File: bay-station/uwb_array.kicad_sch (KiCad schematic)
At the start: 16 parts, among them U4 DW3210, U5 DW3210, U6 DW3210, U7 DW3210

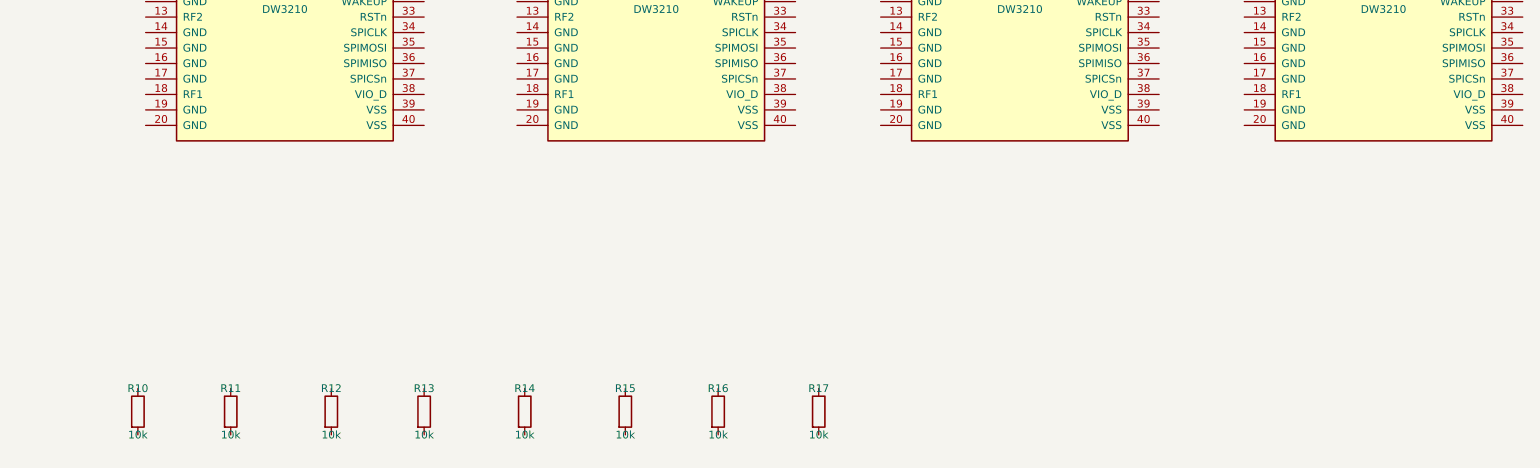
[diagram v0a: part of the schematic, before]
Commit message: Import the DW3210 filtering set from Qorvo's reference design
43 components onto uwb_array.kicad_sch: full per-anchor decoupling, RF1 DC
blocks, RF2 terminations and VDD2a ferrite beads. Placement only, matching
the rest of this board. The sheet previously had 16 components and not one
capacitor.

All values come from the real Qorvo DW3000 Datasheet v1.1, Figure 32
"DW3000 WLCSP Application Circuit" -- Qorvo's own reference design. Figure 32
is an image, so none of it extracts as text; it was read by rendering the
page. Per anchor:

  100nF  VDD1 (29) + VDD2b (23)        [Fig32 C5]
  FB     BLM03PG330SN1D -> VDD2a (28)  [Fig32 FB1]
  4.7nF  VDD2a (28), at the pad        [Fig32 C1]
  4.7nF + 100nF + 10uF  VDD3 (26)      [Fig32 C10/C11/C12]
  220nF  VTX_D (27), cap to GND only   [Fig32 C9]
  100nF  VIO_D (38), cap to GND only   [Fig32 C21]
  2.0pF  RF1 (18) series DC block      [Fig32 C2]
  49R9   RF2 (13) termination          [Fig32 R1, DW3110 inset]

plus a shared +3V3 rail bank of 10uF/100nF/4.7nF [Fig32 C6/C7/C8].

Refdes run in consecutive blocks per anchor: U4 = C40-C47, U5 = C48-C55,
U6 = C56-C63, U7 = C64-C71, rail = C72-C74, beads FB1-FB4, terminations
R33-R36. The table in docs/passives-reference.md was generated from the
file and cross-checked against it, not written by hand.

Two judgment calls worth flagging:

- **The ferrite bead is per anchor, not one on the rail.** Figure 32 shows
  one because it shows one chip. Four transceivers sharing a supply is a
  different problem: a bead each keeps one anchor's TX transient out of the
  others' references, on a board whose product is timestamp accuracy.
- **The 2.0pF on RF1 is not an ordinary DC block** and must not be
  "improved". Qorvo: "these capacitors are a part of the RF transmission
  line, this line was simulated in design and this capacitance value was
  chosen as the result of the simulation." Section 7.3 requires its pads be
  embedded in the track at track width.

Deliberately NOT placed: Figure 3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
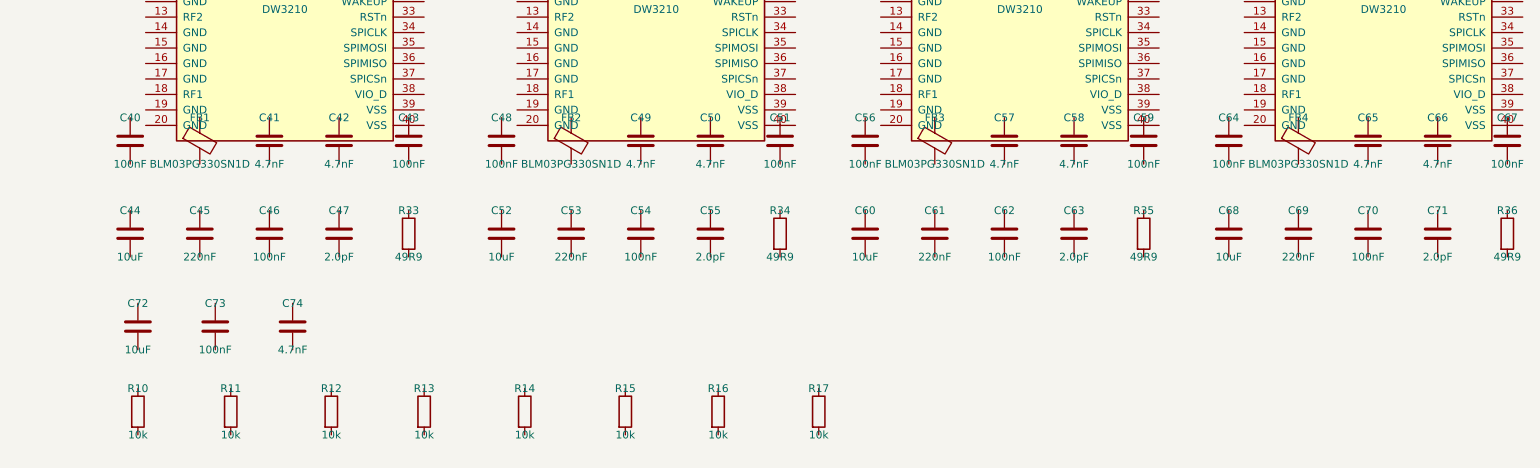
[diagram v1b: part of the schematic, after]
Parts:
- added C40, C43, C46, C48, C51, C54, C56, C59, C62, C64, C67, C70, C73: 100nF, symbol Device:C
- added C41, C42, C49, C50, C57, C58, C65, C66, C74: 4.7nF, symbol Device:C
- added C44, C52, C60, C68, C72: 10uF, symbol Device:C
- added C45, C53, C61, C69: 220nF, symbol Device:C
- added C47, C55, C63, C71: 2.0pF, symbol Device:C
- added FB1, FB2, FB3, FB4: BLM03PG330SN1D, symbol Device:FerriteBead
- added R33, R34, R35, R36: 49R9, symbol Device:R
